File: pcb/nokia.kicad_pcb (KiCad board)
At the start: 4 copper layers, 42.1 x 108 mm, 95 parts, among them J1 Conn_01x07, J2 USB_B_Micro, J20 Conn_01x04_Pin, J3 SM03B-SRSS-TB, J4 Conn_01x06_Pin, J5 Conn_02x10_Top_Bottom, J6 SM03B-SRSS-TB, M1 Vibration, Q1 BC847, SW1 SW_Push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

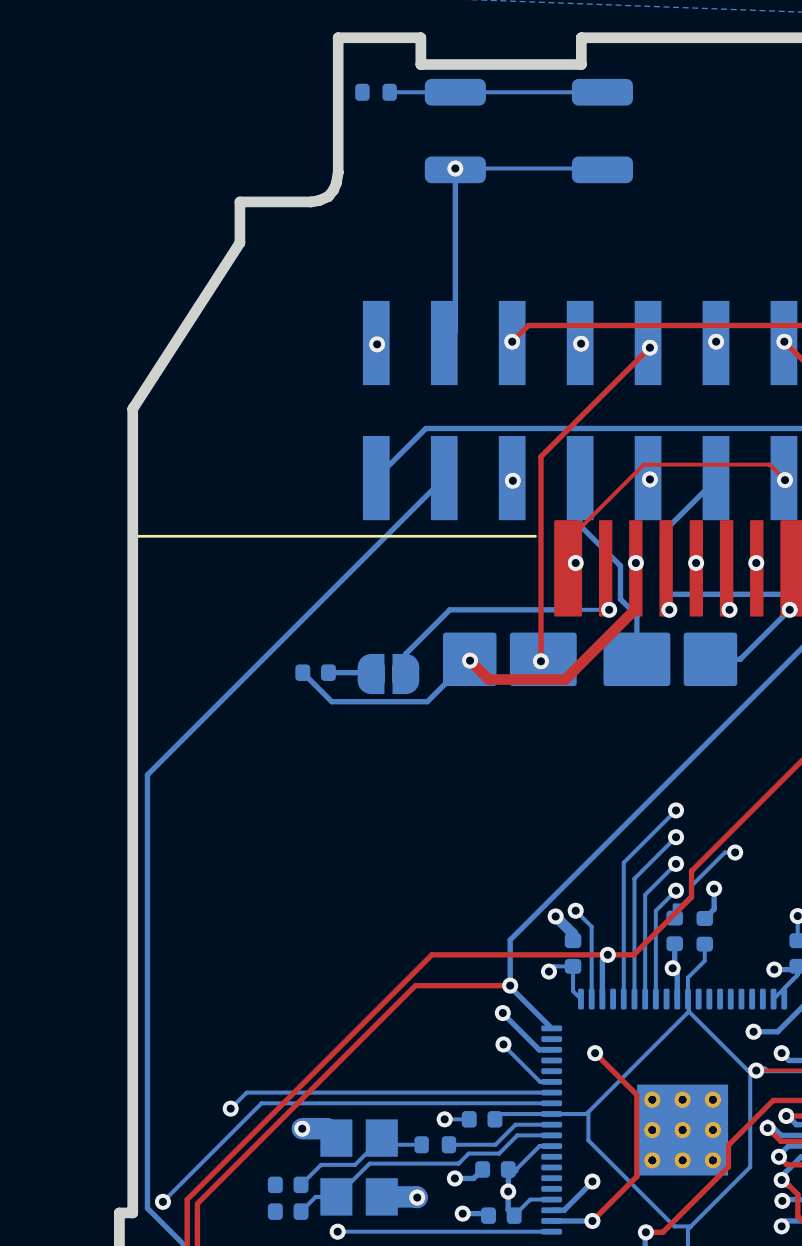
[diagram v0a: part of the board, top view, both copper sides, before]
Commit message: power button can be gpio or run
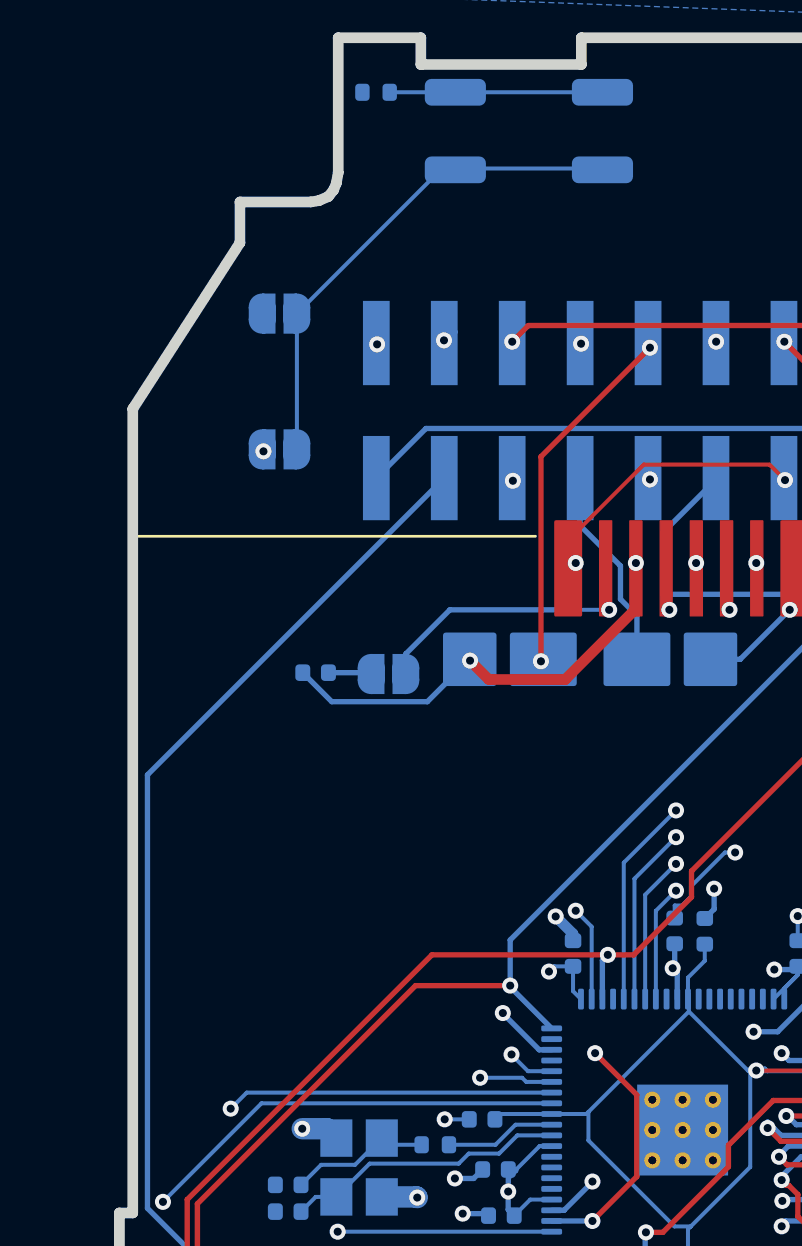
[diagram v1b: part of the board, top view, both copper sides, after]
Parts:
- added JP1: Jumper_2_Open, Jumper:SolderJumper-2_P1.3mm_Open_RoundedPad1.0x1.5mm, B.Cu at (27.4, 29.7)
- added JP2: Jumper_2_Open, Jumper:SolderJumper-2_P1.3mm_Open_RoundedPad1.0x1.5mm, B.Cu at (27.4, 34.8)
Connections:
- SW1 pad 2: /RUN -> Net-(JP1-A)
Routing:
- net /GPIO28: track 0.00 -> 28.2 mm, vias 0 -> 2
- net Net-(JP1-A): track 0.00 -> 18.7 mm
- net /RUN: track 57.3 -> 46.5 mm

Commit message: jlcpcb
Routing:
- net /GPIO22: track 83.7 -> 82.7 mm
- net GND: track 65.2 -> 64.5 mm
- net /RUN: track 46.5 -> 45.8 mm, vias 2 -> 3
- net Net-(JP1-A): track 18.7 -> 18.2 mm

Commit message: make corrections
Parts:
- moved R12 4.74 mm to (51.5, 96.2), turned to 180 degrees
- moved R26 4.22 mm to (49.8, 111.2), turned to -90 degrees
- moved R27 4.22 mm to (58.8, 77.4), turned to -90 degrees
- moved R28 4.13 mm to (58.8, 73.3), turned to -90 degrees
- moved R15 2.72 mm to (31.5, 96.5)
- moved R23 2.54 mm to (24.9, 75.3)
- moved R4 1.40 mm to (54.4, 99.3)
- moved R11 1.38 mm to (54.3, 97.8)
- moved R5 1.30 mm to (50.3, 75.8)
- moved R31 1.30 mm to (36.9, 112.7)
- moved R16 1.25 mm to (50.2, 74.5)
- moved R17 1.25 mm to (44.1, 74.8)
- moved R25 1.22 mm to (54.4, 112.8)
- moved R32 1.20 mm to (30.8, 112.9)
- moved R19 1.15 mm to (40.9, 74.8)
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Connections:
- R11 pad 1: /GPIO32 -> /GPIO30
- R13 pad 2: /GPIO30 -> /GPIO32
- R14 pad 1: /GPIO32 -> /GPIO30
- R16 pad 1: /GPIO32 -> /GPIO30
- R18 pad 2: /GPIO30 -> /GPIO32
- R19 pad 1: /GPIO32 -> /GPIO30
- R21 pad 2: /GPIO30 -> /GPIO32
- R22 pad 1: /GPIO32 -> /GPIO30
- R24 pad 2: /GPIO30 -> /GPIO32
- R25 pad 1: /GPIO32 -> /GPIO30
- R27 pad 2: /GPIO30 -> /GPIO32
- R28 pad 1: /GPIO32 -> /GPIO30
- R30 pad 2: /GPIO30 -> /GPIO32
- R31 pad 1: /GPIO32 -> /GPIO30
- R4 pad 2: /GPIO30 -> /GPIO32
- R5 pad 2: /GPIO30 -> /GPIO32
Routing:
- net +3V3: track 66.5 -> 60.9 mm
- net /GPIO34: track 231.8 -> 227.4 mm
- net Net-(D7-BK): track 1.06 -> 2.23 mm
- net Net-(R6-Pad1): track 7.95 -> 7.18 mm
- net /GPIO30: track 183.9 -> 183.2 mm

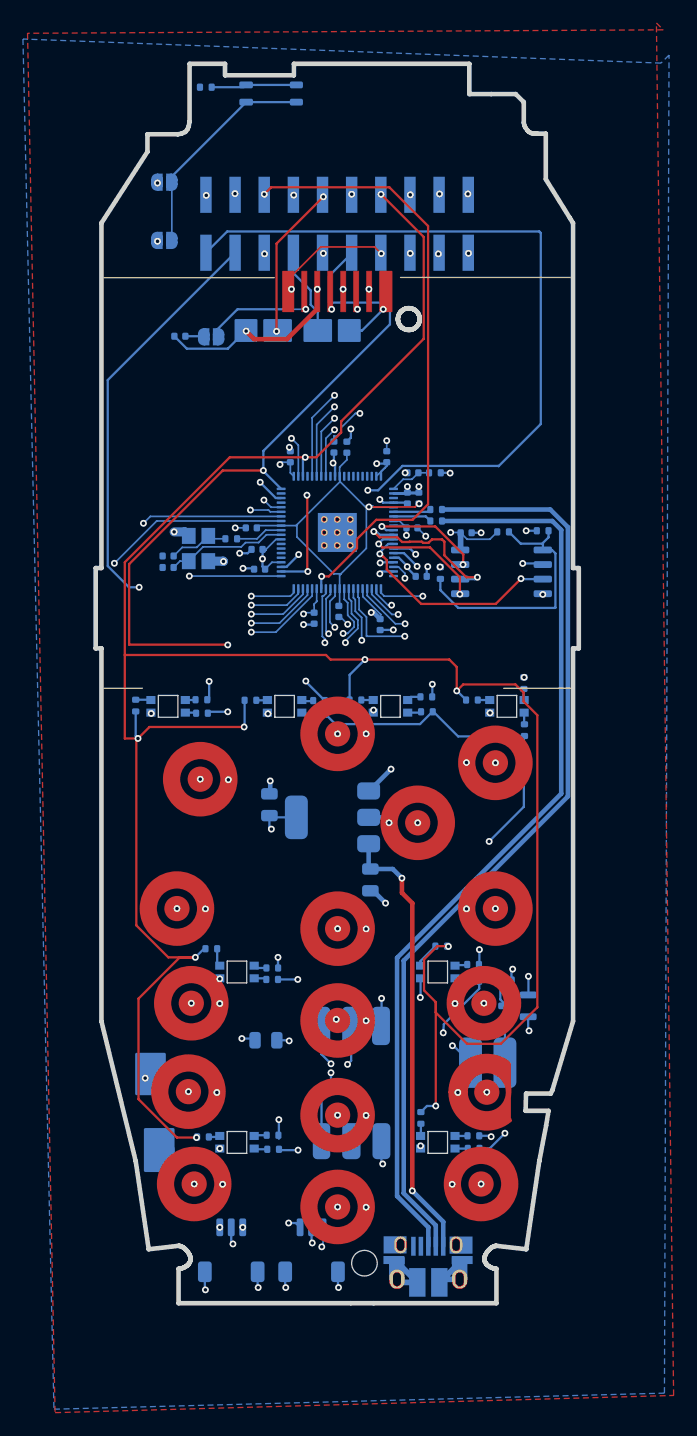
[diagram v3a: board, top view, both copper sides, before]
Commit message: fix clearance for screws, more space for connectors, move LEDs
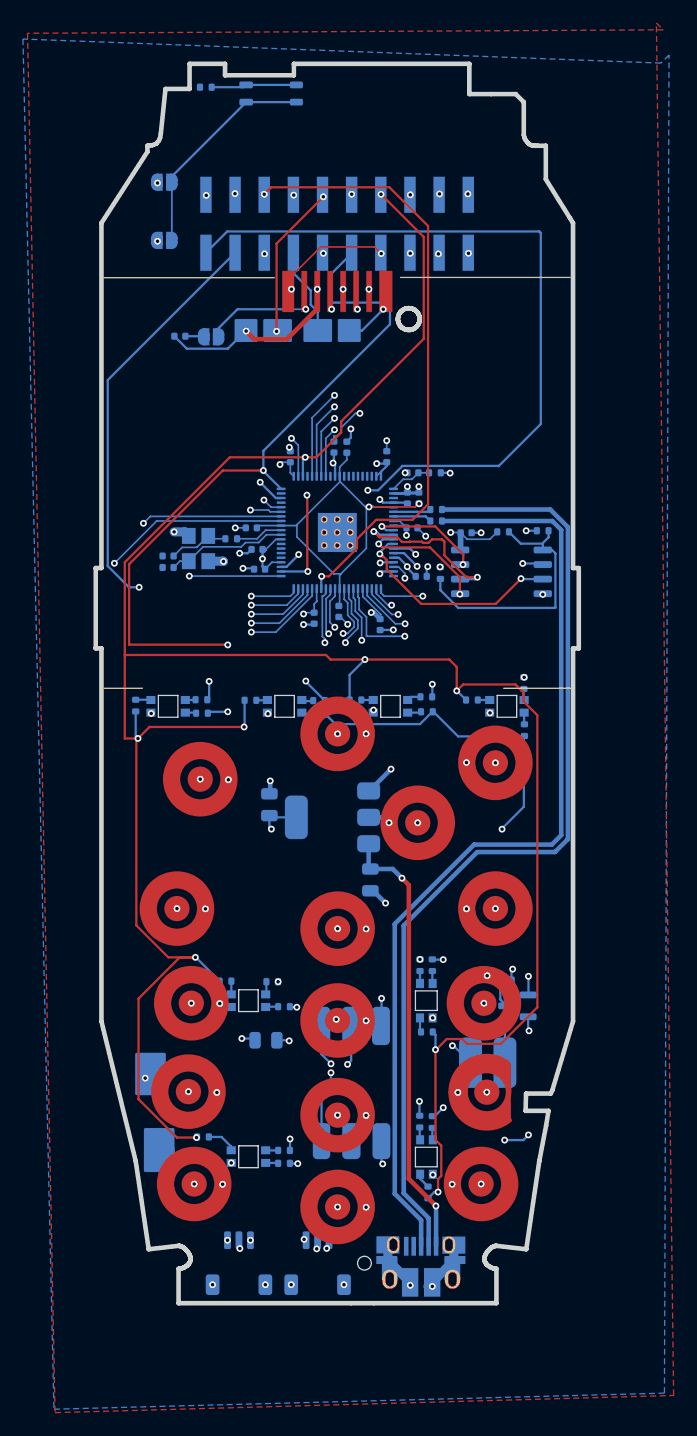
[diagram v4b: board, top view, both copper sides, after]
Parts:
- moved R12 7.58 mm to (50.3, 103.7)
- moved R26 6.53 mm to (50.4, 117.7), turned to 90 degrees
- moved R25 4.84 mm to (49.7, 111.5), turned to -90 degrees
- moved R11 4.63 mm to (49.7, 97.9), turned to -90 degrees
- moved R24 4.27 mm to (50.8, 111.6), turned to 90 degrees
- moved R4 3.84 mm to (50.8, 97.9), turned to 90 degrees
- moved R15 3.08 mm to (32.8, 99.3)
- moved D9 2.69 mm to (35.0, 103.5)
- moved R13 2.59 mm to (37.9, 101.5)
- moved D3 2.01 mm to (52.8, 114.3), turned to -90 degrees
- moved R31 1.66 mm to (37.9, 114.0)
- moved D5 1.60 mm to (35.0, 117.1)
- moved R30 1.55 mm to (37.9, 115.2)
- moved J6 1.31 mm to (33.9, 123.9)
- moved D7 1.30 mm to (52.8, 100.7), turned to -90 degrees
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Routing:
- net /GPIO32: track 206.7 -> 196.3 mm
- net /GPIO30: track 183.2 -> 175.5 mm
- net GND: track 64.5 -> 57.1 mm, vias 35 -> 37
- net /USB_D+: track 80.2 -> 84.1 mm
- net /USB_D-: track 81.3 -> 85.1 mm
- net /GPIO1: track 87.2 -> 85.1 mm
- net /GPIO0: track 96.7 -> 94.7 mm
- net Net-(D5-BK): track 0.86 -> 2.61 mm
- net +3V3: track 60.9 -> 62.6 mm, vias 43 -> 44
- net /GPIO34: track 227.4 -> 226.0 mm
- net /SWCLK: track 82.2 -> 83.3 mm
- net /SWD: track 82.3 -> 83.4 mm
- net Net-(D7-BK): track 2.23 -> 1.14 mm
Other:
- outline, holes or cut-outs redrawn

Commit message: remove prototyping connector
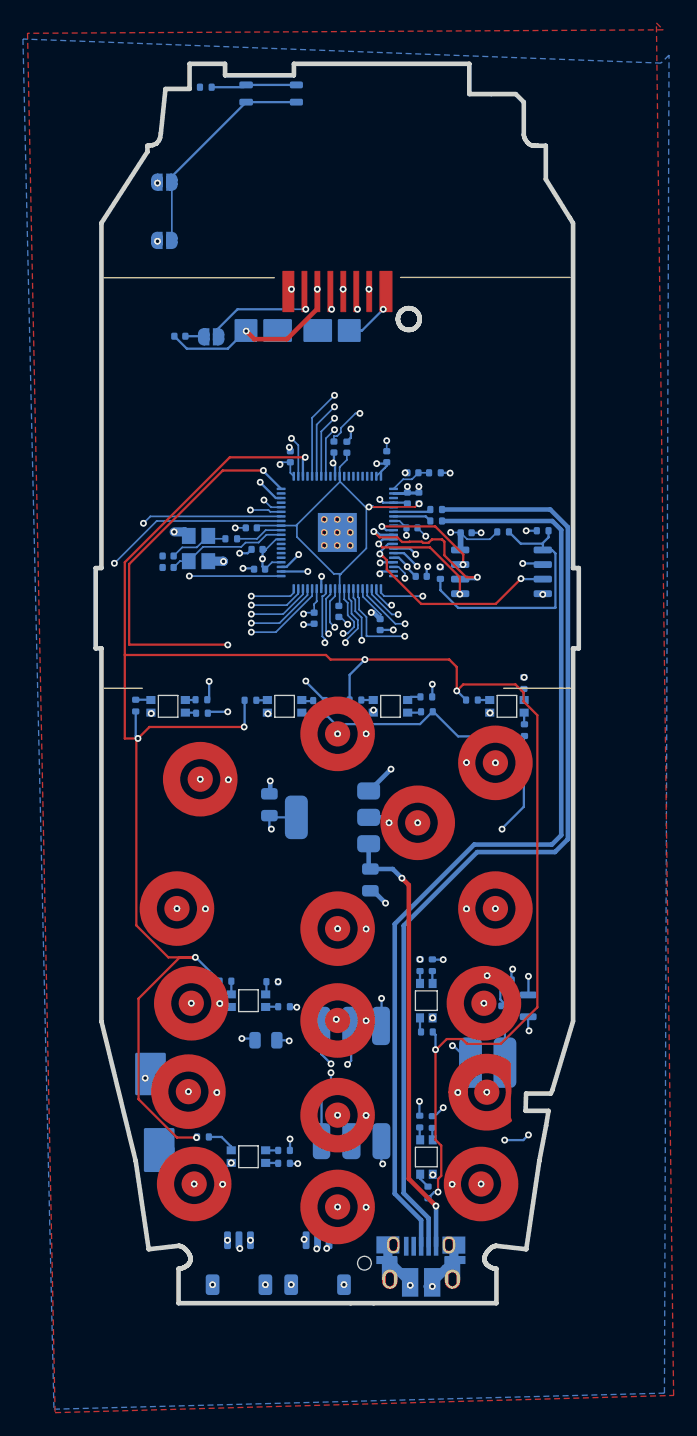
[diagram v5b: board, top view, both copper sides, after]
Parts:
- removed J5: Conn_02x10_Top_Bottom, Connector_PinHeader_2.54mm:PinHeader_2x10_P2.54mm_Vertical_SMD
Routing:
- net /GPIO2: track 120.4 -> 48.1 mm, vias 3 -> 2
- net /GPIO15: track 100.3 -> 47.8 mm, vias 3 -> 2
- net /GPIO23: track 103.6 -> 52.7 mm, vias 3 -> 2
- net /GPIO21: track 102.5 -> 55.3 mm, vias 3 -> 2
- net /GPIO32: track 196.3 -> 166.8 mm
- net /GPIO34: track 226.0 -> 196.6 mm, vias 10 -> 9
- net /GPIO22: track 82.7 -> 53.4 mm, vias 4 -> 2
- net /GPIO30: track 175.5 -> 146.8 mm, vias 10 -> 9
- net Net-(J20-Pin_3): track 13.4 -> 0.00 mm, vias 2 -> 0
- net /GPIO39: track 28.7 -> 15.7 mm, vias 3 -> 2
- net /GPIO37: track 29.3 -> 16.5 mm, vias 3 -> 2
- net /RUN: track 45.8 -> 36.3 mm, vias 3 -> 2
- net /GPIO33: track 28.4 -> 19.3 mm, vias 3 -> 2
- net Net-(J20-Pin_2): track 7.65 -> 0.00 mm
- net /GPIO38: track 25.3 -> 18.0 mm, vias 3 -> 2
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
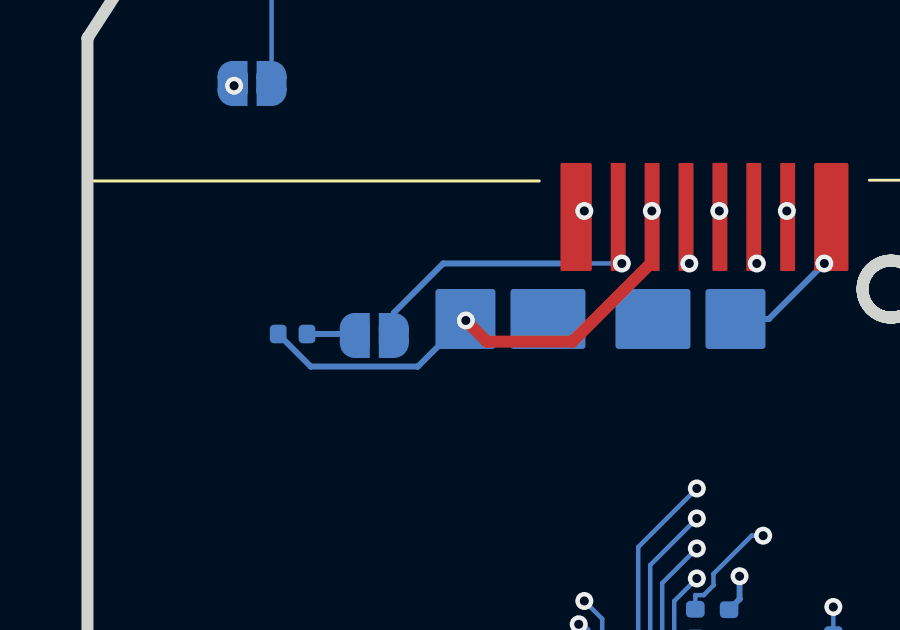
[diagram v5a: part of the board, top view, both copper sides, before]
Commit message: remove display cap jumper
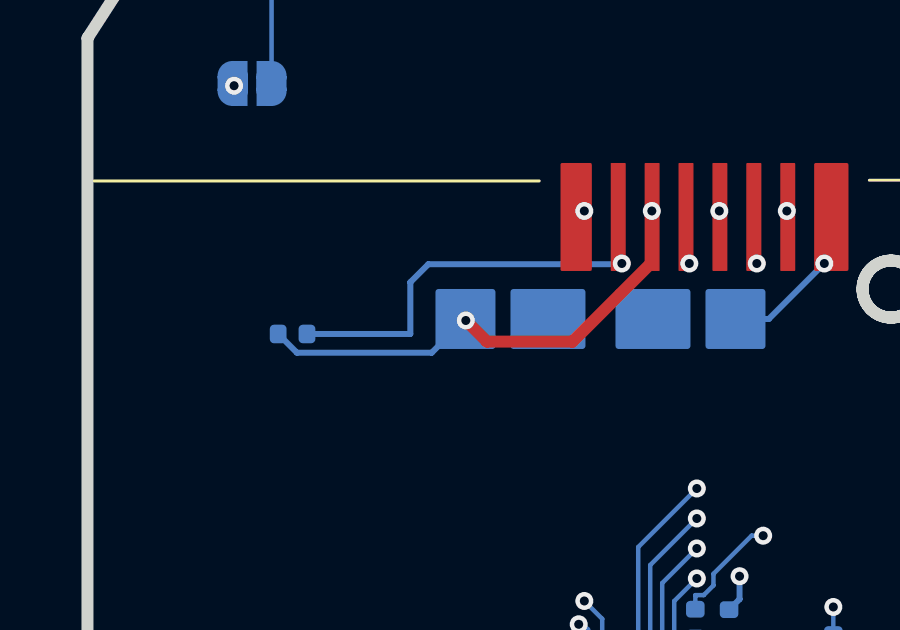
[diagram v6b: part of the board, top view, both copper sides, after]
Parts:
- removed JP17: SolderJumper_2_Open, Jumper:SolderJumper-2_P1.3mm_Open_RoundedPad1.0x1.5mm
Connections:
- C79 pad 2: Net-(JP17-B) -> Net-(J1-Pin_7)
- J20 pad 2: Net-(J20-Pin_2) -> unconnected-(J20-Pin_2-Pad2)
- J20 pad 3: Net-(J20-Pin_3) -> unconnected-(J20-Pin_3-Pad3)
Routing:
- net Net-(J1-Pin_7): track 9.04 -> 12.5 mm
- net Net-(JP17-B): track 1.55 -> 0.00 mm

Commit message: switch
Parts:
- moved SW1 0.26 mm to (36.7, 27.9)
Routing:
- net Net-(JP1-A): track 18.6 -> 19.5 mm
- net Net-(R6-Pad1): track 7.18 -> 7.81 mm
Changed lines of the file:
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@@
 	(footprint "Button_Switch_SMD:power switch"
 		(layer "B.Cu")
-		(at 36.5 27.8 180)
+		(at 36.725 27.925 180)
 		(property "Reference" "SW1"
 			(at -0.05 2.05 0)
@@
 		)
 		(pad "1" smd roundrect
-			(at -2.4285 6.6 180)
-			(size 1.143 0.6)
+			(at -2.6 6.6 180)
+			(size 1.6 1)
 			(layers "B.Cu" "B.Paste" "B.Mask")
 			(roundrect_rratio 0.25)
@@
 		)
 		(pad "1" smd roundrect
-			(at 1.9535 6.6 180)
-			(size 1.193 0.6)
+			(at 2.70175 6.6 180)
+			(size 1.5965 1)
 			(layers "B.Cu" "B.Paste" "B.Mask")
 			(roundrect_rratio 0.25)
@@
 		)
 		(pad "2" smd roundrect
-			(at -2.4285 5.1 180)
-			(size 1.143 0.6)
+			(at -2.6 4.9 180)
+			(size 1.6 1)
 			(layers "B.Cu" "B.Paste" "B.Mask")
 			(roundrect_rratio 0.25)
@@
 		)
 		(pad "2" smd roundrect
-			(at 1.95 5.1 180)
-			(size 1.193 0.6)
+			(at 2.70175 4.9 180)
+			(size 1.5965 1)
 			(layers "B.Cu" "B.Paste" "B.Mask")
 			(roundrect_rratio 0.25)
@@
 	)
 	(segment
-		(start 34.5465 21.2)
-		(end 38.9285 21.2)
+		(start 34.02325 21.325)
+		(end 39.325 21.325)
+		(width 0.2)
+		(layer "B.Cu")
+		(net 16)
+	)
+	(segment
+		(start 33.94825 21.4)
+		(end 34.02325 21.325)
 		(width 0.2)
 		(layer "B.Cu")
@@
 	(segment
 		(start 31.545 21.4)
-		(end 34.3465 21.4)
+		(end 33.94825 21.4)
 		(width 0.2)
 		(layer "B.Cu")
@@
 	)
 	(segment
-		(start 34.55 22.7)
-		(end 28.075 29.175)
+		(start 39.325 23.025)
+		(end 34.02325 23.025)
 		(width 0.2)
 		(layer "B.Cu")
@@
 	)
 	(segment
-		(start 38.9285 22.7)
-		(end 34.55 22.7)
-		(width 0.2)
+		(start 28.075 29.675)
+		(end 34.02325 23.72675)
+		(width 0.15)
+		(layer "B.Cu")
+		(net 103)
+	)
+	(segment
+		(start 34.02325 23.72675)
+		(end 34.02325 23.025)
+		(width 0.15)
 		(layer "B.Cu")
 		(net 103)
